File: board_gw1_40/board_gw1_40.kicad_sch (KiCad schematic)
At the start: 214 parts, among them J1 USB_C_Receptacle, Q1 2N7002, Q10 2N7002, Q11 2N7002, Q12 2N7002, Q13 2N7002, Q14 2N7002, Q15 2N7002, Q16 2N7002, Q17 2N7002, Q18 2N7002, Q19 2N7002, Q2 2N7002, Q20 2N7002, Q21 2N7002, Q22 2N7002, Q23 2N7002, Q24 2N7002, Q25 2N7002, Q26 2N7002, Q27 2N7002, Q28 2N7002, Q29 2N7002, Q3 2N7002, Q30 2N7002, Q31 2N7002, Q32 2N7002, Q33 2N7002, Q34 2N7002, Q35 2N7002, Q36 2N7002, Q37 2N7002, Q38 2N7002, Q39 2N7002, Q4 2N7002, Q40 2N7002, Q41 2N7002, Q5 2N7002, Q6 2N7002, Q7 2N7002, Q8 2N7002, Q9 2N7002, U1 GW1NR-LV9-QN88-C6/I5, U11 FT232H, U2 ESD224DQA, U3 MIC5203-3.3BM5, U4 APS6404L-3SQR-ZR, U5 MIC5504-1.2YM5, U6 TPS562242, U7 W25Q16JVUXIQ, X2 27MHz, Y1 12MHz

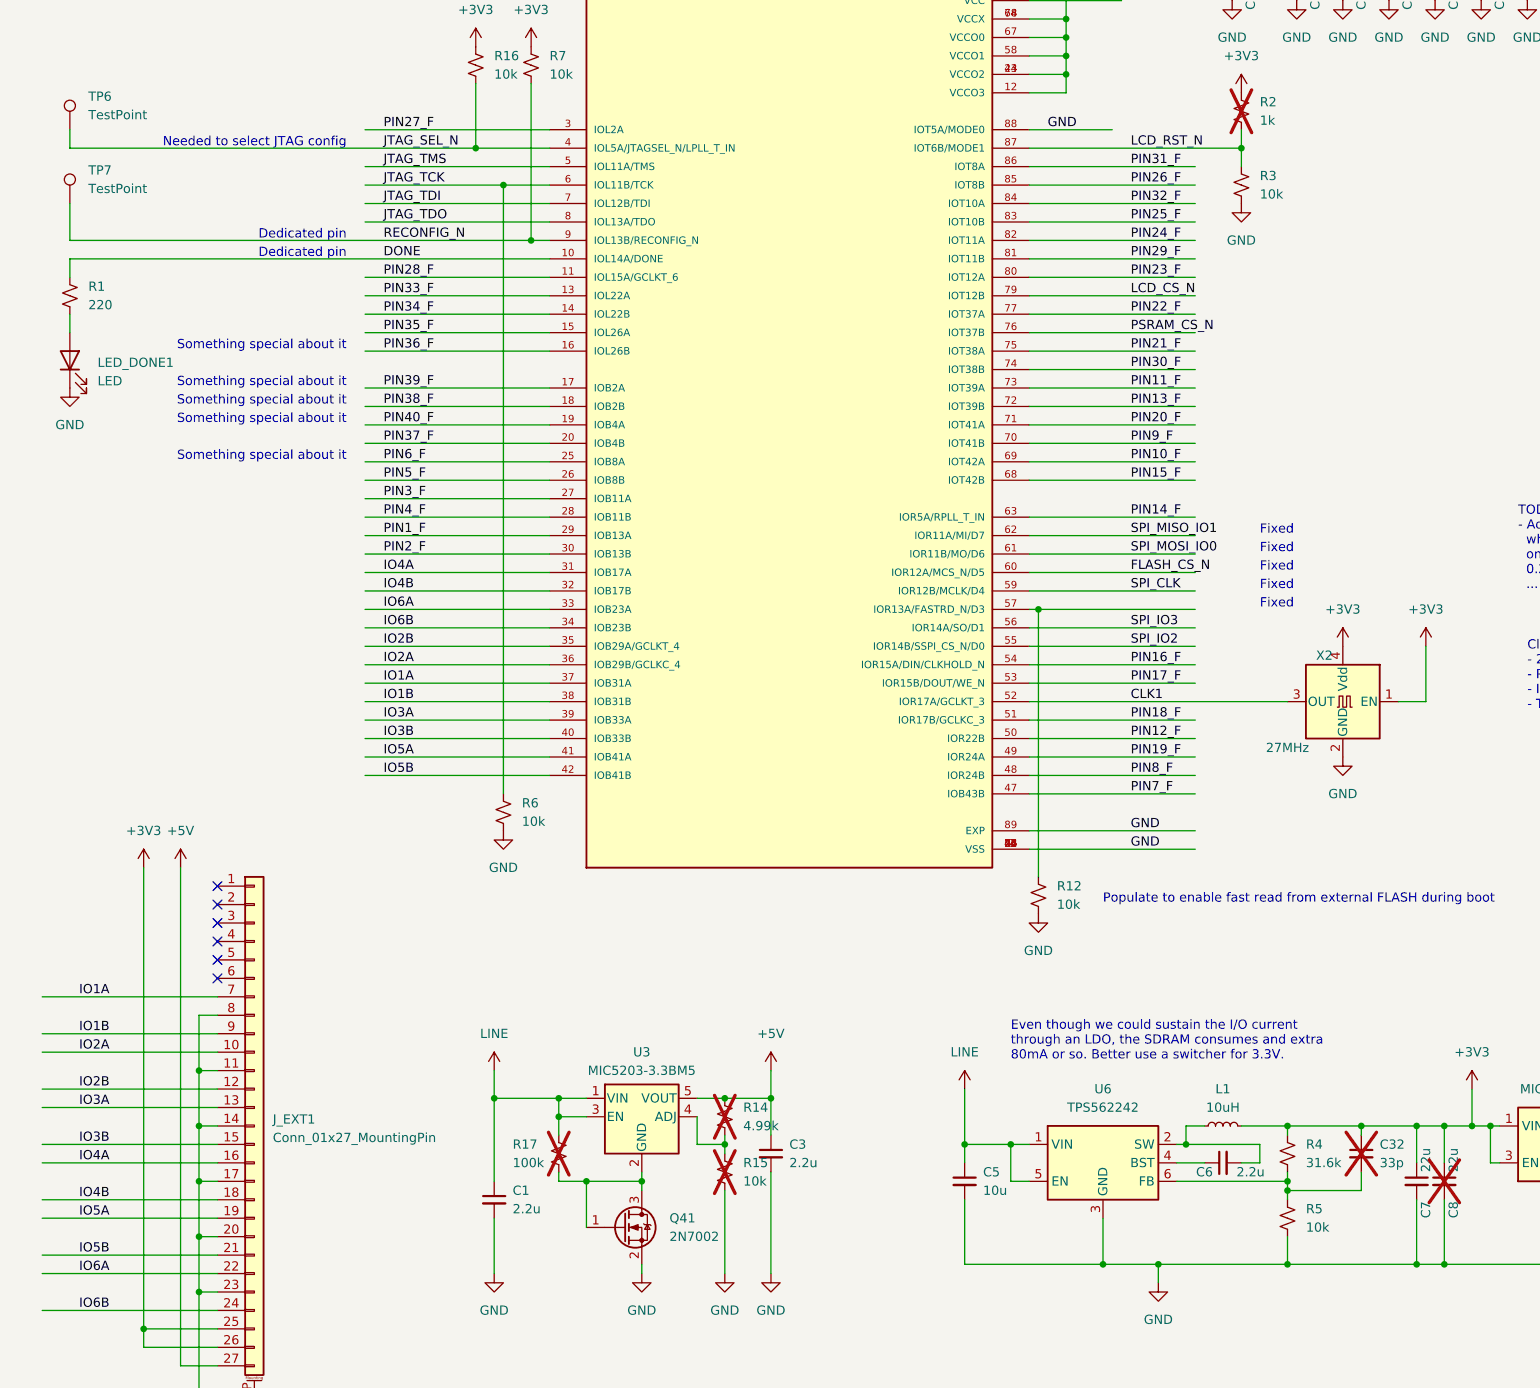
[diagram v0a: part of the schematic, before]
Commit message: Some progress with 40-pin board.
In the end, it might not be any better than the old one.
We shall see...
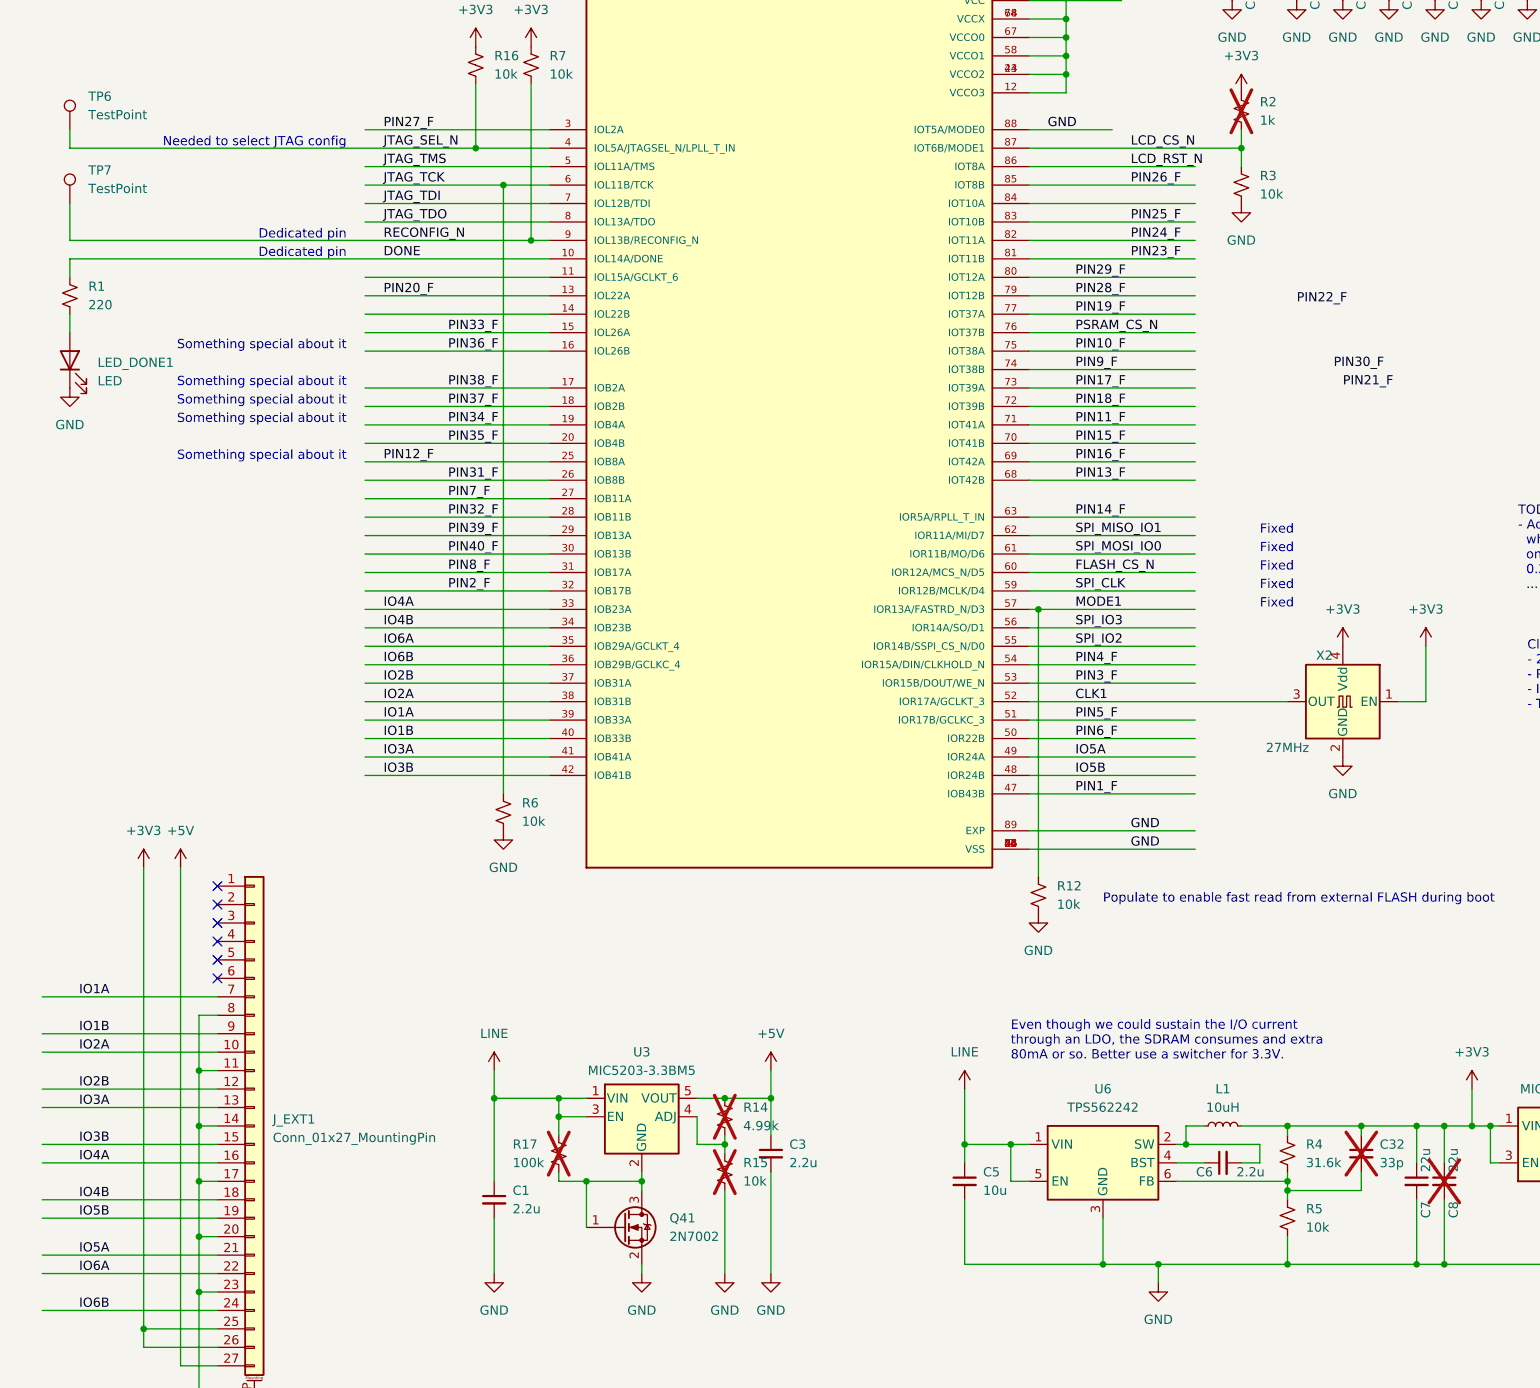
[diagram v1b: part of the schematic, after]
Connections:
- net IO1A: now also U1.39 (IOB33A); no longer U1.37 (IOB31A)
- net IO1B: now also U1.40 (IOB33B); no longer U1.38 (IOB31B)
- net IO2A: now also U1.38 (IOB31B); no longer U1.36 (IOB29B/GCLKC_4)
- net IO2B: now also U1.37 (IOB31A); no longer U1.35 (IOB29A/GCLKT_4)
- net IO3A: now also U1.41 (IOB41A); no longer U1.39 (IOB33A)
- net IO3B: now also U1.42 (IOB41B); no longer U1.40 (IOB33B)
- net IO4A: now also U1.33 (IOB23A); no longer U1.31 (IOB17A)
- net IO4B: now also U1.34 (IOB23B); no longer U1.32 (IOB17B)
- net IO5A: now also J_EXT1.21 (Pin_21), U1.49 (IOR24A); no longer J_EXT1.19 (Pin_19), U1.41 (IOB41A)
- net IO5B: now also J_EXT1.19 (Pin_19), U1.48 (IOR24B); no longer J_EXT1.21 (Pin_21), U1.42 (IOB41B)
- net IO6A: now also U1.35 (IOB29A/GCLKT_4); no longer U1.33 (IOB23A)
- net IO6B: now also U1.36 (IOB29B/GCLKC_4); no longer U1.34 (IOB23B)
- net LCD_CS_N: now also R2.2, R3.1, U1.87 (IOT6B/MODE1); no longer U1.79 (IOT12B)
- net LCD_RST_N: now also U1.86 (IOT8A); no longer R2.2, R3.1, U1.87 (IOT6B/MODE1)
- net PIN10_F: now also U1.75 (IOT38A); no longer U1.69 (IOT42A)
- net PIN11_F: now also U1.71 (IOT41A); no longer U1.73 (IOT39A)
- net PIN12_F: now also U1.25 (IOB8A); no longer U1.50 (IOR22B)
- net PIN13_F: now also U1.68 (IOT42B); no longer U1.72 (IOT39B)
- net PIN15_F: now also U1.70 (IOT41B); no longer U1.68 (IOT42B)
- net PIN16_F: now also U1.69 (IOT42A); no longer U1.54 (IOR15A/DIN/CLKHOLD_N)
- net PIN17_F: now also U1.73 (IOT39A); no longer U1.53 (IOR15B/DOUT/WE_N)
- net PIN18_F: now also U1.72 (IOT39B); no longer U1.51 (IOR17B/GCLKC_3)
- net PIN19_F: now also U1.77 (IOT37A); no longer U1.49 (IOR24A)
- net PIN1_F: now also U1.47 (IOB43B); no longer U1.29 (IOB13A)
- net PIN20_F: now also U1.13 (IOL22A); no longer U1.71 (IOT41A)
- net PIN21_F: no longer U1.75 (IOT38A)
- net PIN22_F: no longer U1.77 (IOT37A)
- net PIN23_F: now also U1.81 (IOT11B); no longer U1.80 (IOT12A)
- net PIN28_F: now also U1.79 (IOT12B); no longer U1.11 (IOL15A/GCLKT_6)
- net PIN29_F: now also U1.80 (IOT12A); no longer U1.81 (IOT11B)
- net PIN2_F: now also U1.32 (IOB17B); no longer U1.30 (IOB13B)
- net PIN30_F: no longer U1.74 (IOT38B)
- net PIN31_F: now also U1.26 (IOB8B); no longer U1.86 (IOT8A)
- net PIN32_F: now also U1.28 (IOB11B); no longer U1.84 (IOT10A)
- net PIN33_F: now also U1.15 (IOL26A); no longer U1.13 (IOL22A)
- net PIN34_F: now also U1.19 (IOB4A); no longer U1.14 (IOL22B)
- net PIN35_F: now also U1.20 (IOB4B); no longer U1.15 (IOL26A)
- net PIN37_F: now also U1.18 (IOB2B); no longer U1.20 (IOB4B)
- net PIN38_F: now also U1.17 (IOB2A); no longer U1.18 (IOB2B)
- net PIN39_F: now also U1.29 (IOB13A); no longer U1.17 (IOB2A)
- net PIN3_F: now also U1.53 (IOR15B/DOUT/WE_N); no longer U1.27 (IOB11A)
- net PIN40_F: now also U1.30 (IOB13B); no longer U1.19 (IOB4A)
- net PIN4_F: now also U1.54 (IOR15A/DIN/CLKHOLD_N); no longer U1.28 (IOB11B)
- net PIN5_F: now also U1.51 (IOR17B/GCLKC_3); no longer U1.26 (IOB8B)
- net PIN6_F: now also U1.50 (IOR22B); no longer U1.25 (IOB8A)
- net PIN7_F: now also U1.27 (IOB11A); no longer U1.47 (IOB43B)
- net PIN8_F: now also U1.31 (IOB17A); no longer U1.48 (IOR24B)
- net PIN9_F: now also U1.74 (IOT38B); no longer U1.70 (IOT41B)
- net MODE1: now reaches R12.1, U1.57 (IOR13A/FASTRD_N/D3)
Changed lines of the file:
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@@
 	)
 	(label "PIN23_F"
-		(at 182.88 87.63 0)
+		(at 182.88 85.09 0)
 		(effects
 			(font
@@
 	)
 	(label "PIN37_F"
-		(at 80.01 110.49 0)
+		(at 88.9 105.41 0)
 		(effects
 			(font
@@
 	)
 	(label "IO1A"
-		(at 80.01 143.51 0)
+		(at 80.01 148.59 0)
 		(effects
 			(font
@@
 	)
 	(label "IO6B"
-		(at 80.01 135.89 0)
+		(at 80.01 140.97 0)
 		(effects
 			(font
@@
 	)
 	(label "IO5B"
-		(at 38.1 222.25 0)
+		(at 38.1 217.17 0)
 		(effects
 			(font
@@
 	)
 	(label "PIN16_F"
-		(at 182.88 140.97 0)
+		(at 175.26 113.03 0)
 		(effects
 			(font
@@
 	)
 	(label "PIN13_F"
-		(at 182.88 105.41 0)
+		(at 175.26 115.57 0)
 		(effects
 			(font
@@
 	)
 	(label "PIN14_F"
-		(at 182.88 120.65 0)
+		(at 175.26 120.65 0)
 		(effects
 			(font
@@
 	)
 	(label "SPI_CLK"
-		(at 182.88 130.81 0)
+		(at 175.26 130.81 0)
 		(effects
 			(font
@@
 	)
 	(label "PIN11_F"
-		(at 182.88 102.87 0)
+		(at 175.26 107.95 0)
 		(effects
 			(font
@@
 	)
 	(label "PIN10_F"
-		(at 182.88 113.03 0)
+		(at 175.26 97.79 0)
 		(effects
 			(font
@@
 	)
 	(label "PIN12_F"
-		(at 182.88 151.13 0)
+		(at 80.01 113.03 0)
 		(effects
 			(font
@@
 	)
 	(label "PIN31_F"
-		(at 182.88 72.39 0)
+		(at 88.9 115.57 0)
 		(effects
 			(font
@@
 	)
 	(label "PIN32_F"
-		(at 182.88 77.47 0)
+		(at 88.9 120.65 0)
 		(effects
 			(font
@@
 	)
 	(label "IO2B"
-		(at 80.01 138.43 0)
+		(at 80.01 143.51 0)
 		(effects
 			(font
@@
 	)
 	(label "PSRAM_CS_N"
-		(at 182.88 95.25 0)
+		(at 175.26 95.25 0)
 		(effects
 			(font
@@
 	)
 	(label "IO3A"
-		(at 80.01 148.59 0)
+		(at 80.01 153.67 0)
 		(effects
 			(font
@@
 	)
 	(label "PIN7_F"
-		(at 182.88 158.75 0)
+		(at 88.9 118.11 0)
 		(effects
 			(font
@@
 	)
 	(label "PIN39_F"
-		(at 80.01 102.87 0)
+		(at 88.9 123.19 0)
 		(effects
 			(font
@@
 	)
 	(label "PIN19_F"
-		(at 182.88 153.67 0)
+		(at 175.26 92.71 0)
 		(effects
 			(font
@@
 	)
 	(label "PIN22_F"
-		(at 182.88 92.71 0)
+		(at 205.74 91.44 0)
 		(effects
 			(font
@@
 	)
 	(label "LCD_CS_N"
-		(at 182.88 90.17 0)
+		(at 182.88 69.85 0)
 		(effects
 			(font
@@
 	)
 	(label "IO5A"
-		(at 80.01 153.67 0)
+		(at 175.26 153.67 0)
 		(effects
 			(font
@@
 	)
 	(label "PIN18_F"
-		(at 182.88 148.59 0)
+		(at 175.26 105.41 0)
 		(effects
 			(font
@@
 	)
 	(label "PIN30_F"
-		(at 182.88 100.33 0)
+		(at 210.82 100.33 0)
 		(effects
 			(font
@@
 	)
 	(label "PIN6_F"
-		(at 80.01 113.03 0)
+		(at 175.26 151.13 0)
 		(effects
 			(font
@@
 	)
 	(label "PIN20_F"
-		(at 182.88 107.95 0)
+		(at 80.01 90.17 0)
 		(effects
 			(font
@@
 	)
 	(label "PIN29_F"
-		(at 182.88 85.09 0)
+		(at 175.26 87.63 0)
 		(effects
 			(font
@@
 	)
 	(label "PIN40_F"
-		(at 80.01 107.95 0)
+		(at 88.9 125.73 0)
 		(effects
 			(font
@@
 	)
 	(label "PIN33_F"
-		(at 80.01 90.17 0)
+		(at 88.9 95.25 0)
 		(effects
 			(font
@@
 		)
 	)
+	(label "MODE1"
+		(at 175.26 133.35 0)
+		(effects
+			(font
+				(size 1.27 1.27)
+			)
+			(justify left bottom)
+		)
+	)
 	(label "IO5B"
-		(at 80.01 156.21 0)
+		(at 175.26 156.21 0)
 		(effects
 			(font
@@
 	)
 	(label "PIN34_F"
-		(at 80.01 92.71 0)
+		(at 88.9 107.95 0)
 		(effects
 			(font
@@
 	)
 	(label "PIN1_F"
-		(at 80.01 123.19 0)
+		(at 175.26 158.75 0)
 		(effects
 			(font
@@
 	)
 	(label "IO2A"
-		(at 80.01 140.97 0)
+		(at 80.01 146.05 0)
 		(effects
 			(font
@@
 	)
 	(label "LCD_RST_N"
-		(at 182.88 69.85 0)
+		(at 182.88 72.39 0)
 		(effects
 			(font
@@
 	)
 	(label "SPI_MISO_IO1"
-		(at 182.88 123.19 0)
+		(at 175.26 123.19 0)
 		(effects
 			(font
@@
 	)
 	(label "PIN38_F"
-		(at 80.01 105.41 0)
+		(at 88.9 102.87 0)
 		(effects
 			(font
@@
 	)
 	(label "IO1B"
-		(at 80.01 146.05 0)
+		(at 80.01 151.13 0)
 		(effects
 			(font
@@
 	)
 	(label "PIN5_F"
-		(at 80.01 115.57 0)
+		(at 175.26 148.59 0)
 		(effects
 			(font
@@
 	)
 	(label "PIN35_F"
-		(at 80.01 95.25 0)
+		(at 88.9 110.49 0)
 		(effects
 			(font
@@
 	)
 	(label "PIN21_F"
-		(at 182.88 97.79 0)
+		(at 212.09 102.87 0)
 		(effects
 			(font
@@
 	)
 	(label "SPI_IO2"
-		(at 182.88 138.43 0)
+		(at 175.26 138.43 0)
 		(effects
 			(font
@@
 	)
 	(label "SPI_MOSI_IO0"
-		(at 182.88 125.73 0)
+		(at 175.26 125.73 0)
 		(effects
 			(font
@@
 	)
 	(label "PIN2_F"
-		(at 80.01 125.73 0)
+		(at 88.9 130.81 0)
 		(effects
 			(font
@@
 	)
 	(label "PIN9_F"
-		(at 182.88 110.49 0)
+		(at 175.26 100.33 0)
 		(effects
 			(font
@@
 	)
 	(label "IO4A"
-		(at 80.01 128.27 0)
+		(at 80.01 133.35 0)
 		(effects
 			(font
@@
 	)
 	(label "FLASH_CS_N"
-		(at 182.88 128.27 0)
+		(at 175.26 128.27 0)
 		(effects
 			(font
@@
 	)
 	(label "PIN3_F"
-		(at 80.01 118.11 0)
+		(at 175.26 143.51 0)
 		(effects
 			(font
@@
 	)
 	(label "PIN8_F"
-		(at 182.88 156.21 0)
+		(at 88.9 128.27 0)
 		(effects
 			(font
@@
 	)
 	(label "PIN4_F"
-		(at 80.01 120.65 0)
+		(at 175.26 140.97 0)
 		(effects
 			(font
@@
 	)
 	(label "PIN36_F"
-		(at 80.01 97.79 0)
+		(at 88.9 97.79 0)
 		(effects
 			(font
@@
 	)
 	(label "IO3B"
-		(at 80.01 151.13 0)
+		(at 80.01 156.21 0)
 		(effects
 			(font
@@
 	)
 	(label "IO4B"
-		(at 80.01 130.81 0)
+		(at 80.01 135.89 0)
 		(effects
 			(font
@@
 	)
 	(label "PIN15_F"
-		(at 182.88 115.57 0)
+		(at 175.26 110.49 0)
 		(effects
 			(font
@@
 	)
 	(label "IO5A"
-		(at 38.1 217.17 0)
+		(at 38.1 222.25 0)
 		(effects
 			(font
@@
 	)
 	(label "IO6A"
-		(at 80.01 133.35 0)
+		(at 80.01 138.43 0)
 		(effects
 			(font
@@
 	)
 	(label "SPI_IO3"
-		(at 182.88 135.89 0)
+		(at 175.26 135.89 0)
 		(effects
 			(font
@@
 	)
 	(label "PIN28_F"
-		(at 80.01 87.63 0)
+		(at 175.26 90.17 0)
 		(effects
 			(font
@@
 	)
 	(label "PIN17_F"
-		(at 182.88 143.51 0)
+		(at 175.26 102.87 0)
 		(effects
 			(font
@@
 	)
 	(label "CLK1"
-		(at 182.88 146.05 0)
-		(effects
-			(font
+		(at 175.26 146.05 0)
+		(effects
+			(font
